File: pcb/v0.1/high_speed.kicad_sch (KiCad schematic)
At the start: 14 parts, among them J1 USB_C_Receptacle_fw, J2 USB_C_Receptacle_fw, J3 690-019-298-412, J4 Conn_01x22_Female, U1 AP22653W6, U2 RT9742SNGV

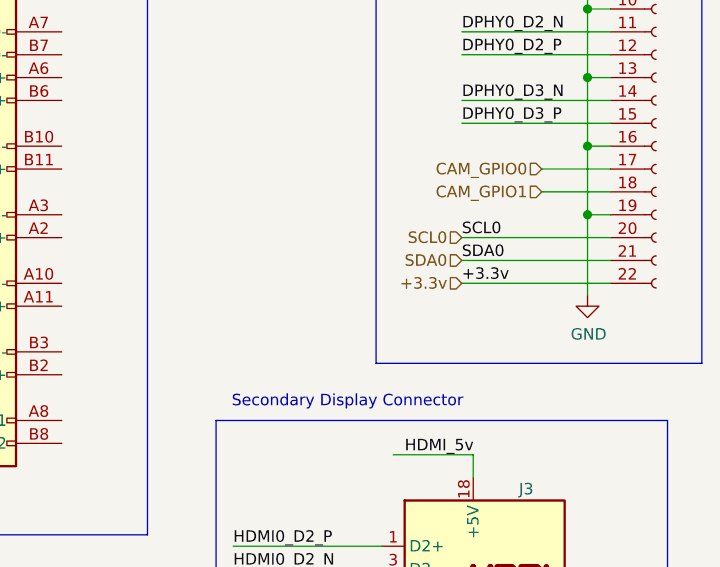
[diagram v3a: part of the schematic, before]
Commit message: Clean up main page and power rails
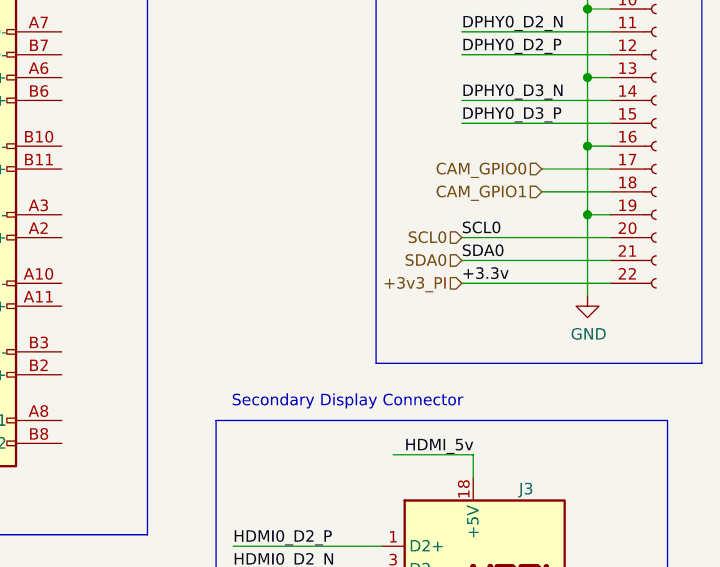
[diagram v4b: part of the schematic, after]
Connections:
- net +3.3v renamed +3v3_PI
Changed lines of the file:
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@@
 		)
 	)
-	(hierarchical_label "+3.3v"
+	(hierarchical_label "+3v3_PI"
 		(shape input)
 		(at 254 76.2 180)

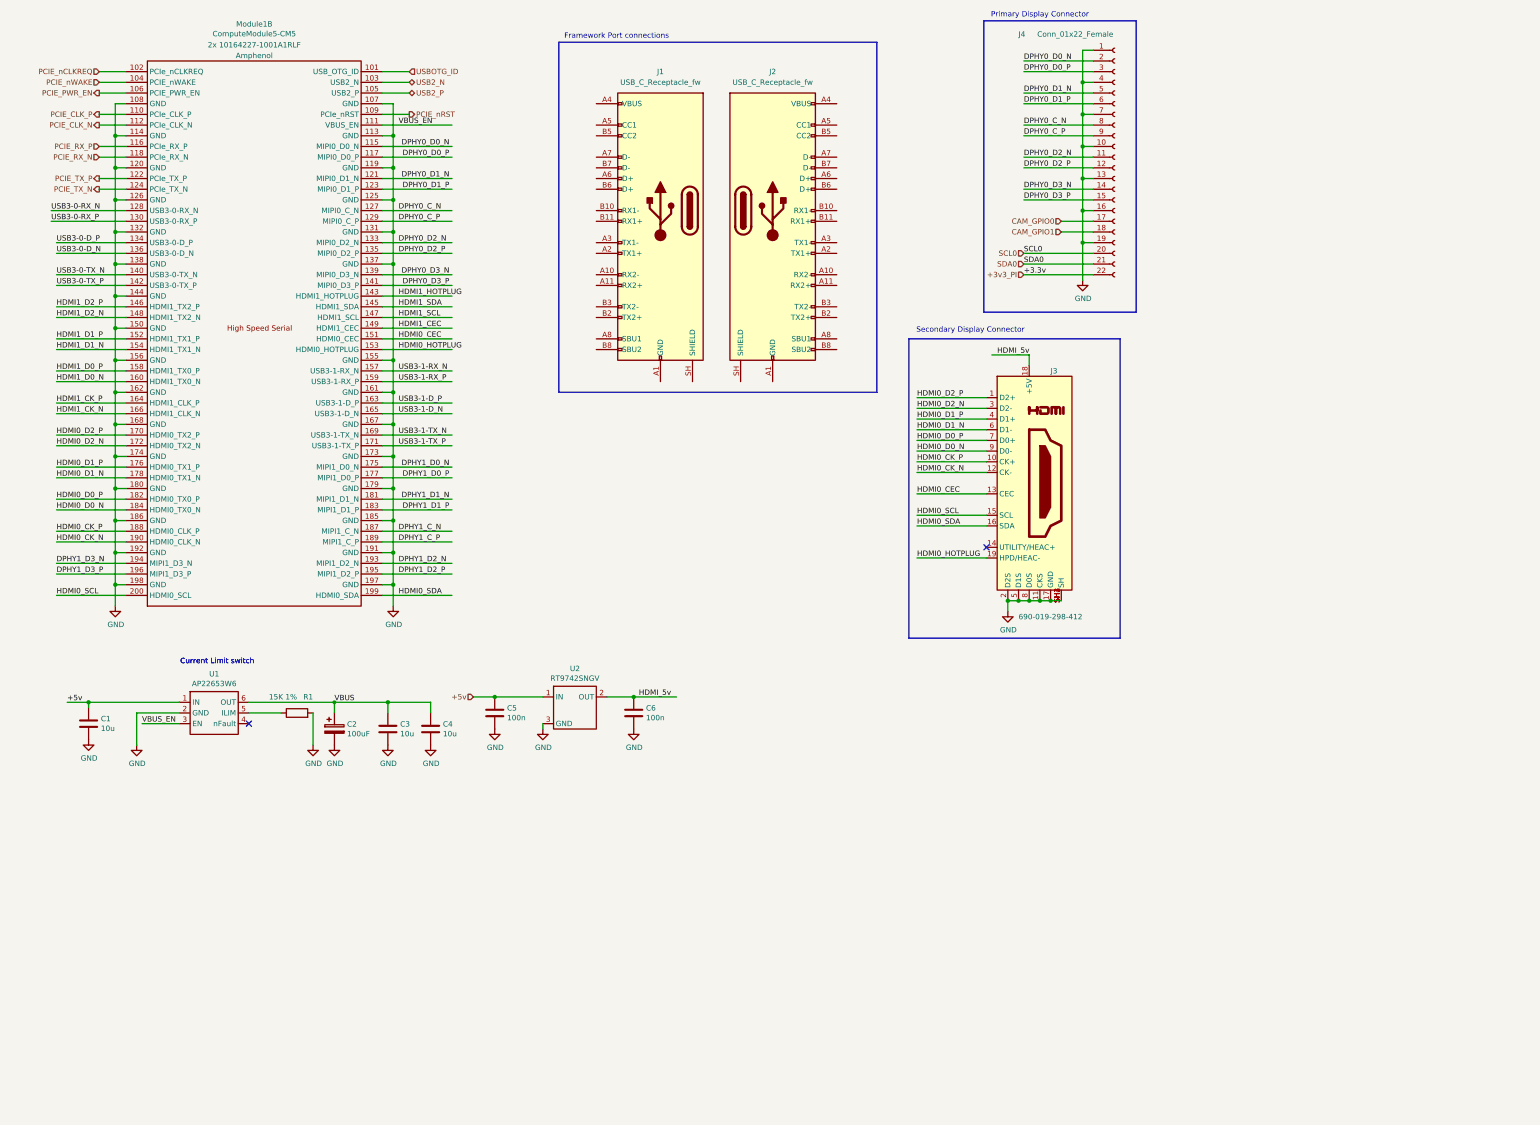
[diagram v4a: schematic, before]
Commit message: Add pullup for nRESET of the nRF.
Also re-annotated all of the symbol numbers as they were starting to get
out of hand.
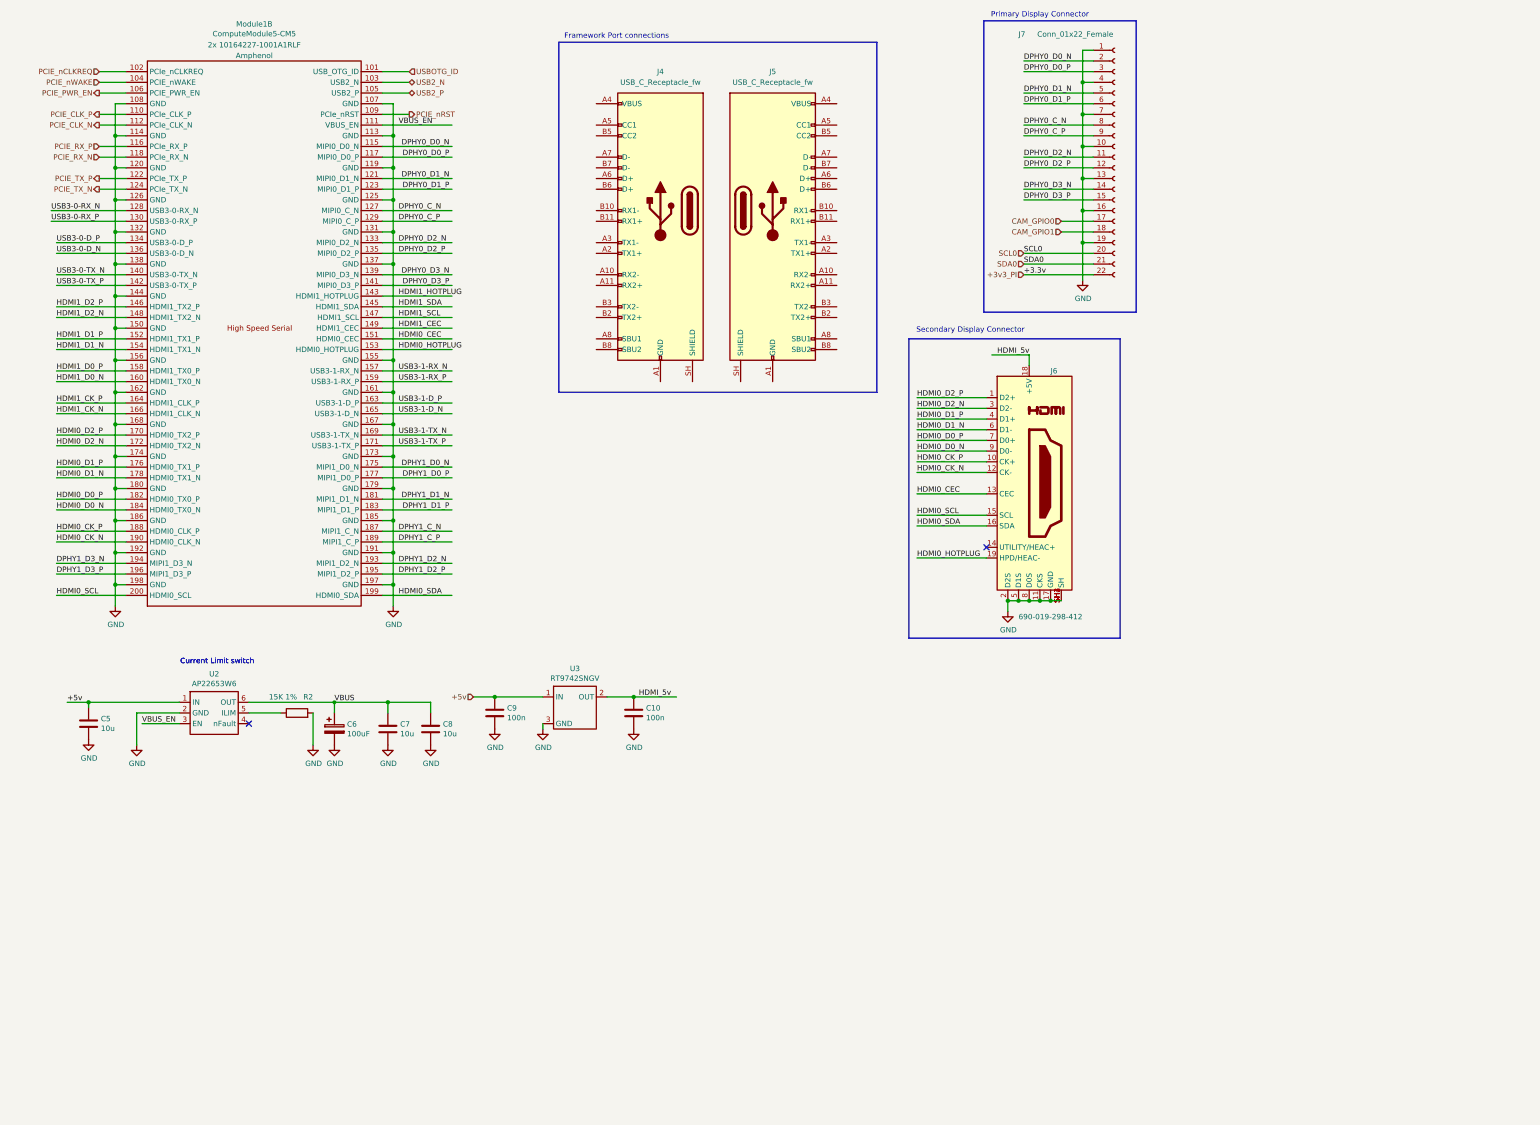
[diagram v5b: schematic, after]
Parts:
- renumbered C6 to C10, C1 to C5, C2 to C6, C3 to C7, C4 to C8, C5 to C9, J1 to J4, J2 to J5, J3 to J6, J4 to J7, R1 to R2, U1 to U2, U2 to U3
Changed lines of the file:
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@@
 		(in_pos_files yes)
 		(dnp no)
-		(property "Reference" "#PWR05"
+		(property "Reference" "#PWR010"
 			(at 90.17 194.31 0)
 			(hide yes)
@@
 			(project "mainboard"
 				(path "/5b8aa782-5c3d-43e7-a869-3bd000015f52/8e613e76-cfa9-4d70-9fba-6dbea9bbdbc9"
-					(reference "#PWR05")
+					(reference "#PWR010")
 					(unit 1)
 				)
@@
 		(in_pos_files yes)
 		(dnp no)
-		(property "Reference" "#PWR01"
+		(property "Reference" "#PWR06"
 			(at 31.75 193.04 0)
 			(hide yes)
@@
 			(project "mainboard"
 				(path "/5b8aa782-5c3d-43e7-a869-3bd000015f52/8e613e76-cfa9-4d70-9fba-6dbea9bbdbc9"
-					(reference "#PWR01")
+					(reference "#PWR06")
 					(unit 1)
 				)
@@
 		(in_pos_files yes)
 		(dnp no)
-		(property "Reference" "#PWR010"
+		(property "Reference" "#PWR015"
 			(at 139.7 190.5 0)
 			(hide yes)
@@
 			(project "mainboard"
 				(path "/5b8aa782-5c3d-43e7-a869-3bd000015f52/8e613e76-cfa9-4d70-9fba-6dbea9bbdbc9"
-					(reference "#PWR010")
+					(reference "#PWR015")
 					(unit 1)
 				)
@@
 		(in_pos_files yes)
 		(dnp no)
-		(property "Reference" "J4"
+		(property "Reference" "J7"
 			(at 252.73 19.05 0)
 			(show_name no)
@@
 			(project "mainboard"
 				(path "/5b8aa782-5c3d-43e7-a869-3bd000015f52/8e613e76-cfa9-4d70-9fba-6dbea9bbdbc9"
-					(reference "J4")
+					(reference "J7")
 					(unit 1)
 				)
@@
 		(in_pos_files yes)
 		(dnp no)
-		(property "Reference" "J1"
+		(property "Reference" "J4"
 			(at 167.64 27.94 0)
 			(show_name no)
@@
 			(project "mainboard"
 				(path "/5b8aa782-5c3d-43e7-a869-3bd000015f52/8e613e76-cfa9-4d70-9fba-6dbea9bbdbc9"
-					(reference "J1")
+					(reference "J4")
 					(unit 1)
 				)
@@
 		(in_pos_files yes)
 		(dnp no)
-		(property "Reference" "#PWR03"
+		(property "Reference" "#PWR08"
 			(at 43.18 194.31 0)
 			(hide yes)
@@
 			(project "mainboard"
 				(path "/5b8aa782-5c3d-43e7-a869-3bd000015f52/8e613e76-cfa9-4d70-9fba-6dbea9bbdbc9"
-					(reference "#PWR03")
+					(reference "#PWR08")
 					(unit 1)
 				)
@@
 		(in_pos_files yes)
 		(dnp no)
-		(property "Reference" "C4"
+		(property "Reference" "C8"
 			(at 115.951 182.9816 0)
 			(show_name no)
@@
 			(project "mainboard"
 				(path "/5b8aa782-5c3d-43e7-a869-3bd000015f52/8e613e76-cfa9-4d70-9fba-6dbea9bbdbc9"
-					(reference "C4")
+					(reference "C8")
 					(unit 1)
 				)
@@
 		(in_pos_files yes)
 		(dnp no)
-		(property "Reference" "#PWR08"
+		(property "Reference" "#PWR013"
 			(at 113.03 194.31 0)
 			(hide yes)
@@
 			(project "mainboard"
 				(path "/5b8aa782-5c3d-43e7-a869-3bd000015f52/8e613e76-cfa9-4d70-9fba-6dbea9bbdbc9"
-					(reference "#PWR08")
+					(reference "#PWR013")
 					(unit 1)
 				)
@@
 		(in_pos_files yes)
 		(dnp no)
-		(property "Reference" "#PWR013"
+		(property "Reference" "#PWR018"
 			(at 267.97 83.82 0)
 			(hide yes)
@@
 			(project "mainboard"
 				(path "/5b8aa782-5c3d-43e7-a869-3bd000015f52/8e613e76-cfa9-4d70-9fba-6dbea9bbdbc9"
-					(reference "#PWR013")
+					(reference "#PWR018")
 					(unit 1)
 				)
@@
 		(in_pos_files yes)
 		(dnp no)
-		(property "Reference" "U1"
+		(property "Reference" "U2"
 			(at 61.595 171.069 0)
 			(show_name no)
@@
 			(project "mainboard"
 				(path "/5b8aa782-5c3d-43e7-a869-3bd000015f52/8e613e76-cfa9-4d70-9fba-6dbea9bbdbc9"
-					(reference "U1")
+					(reference "U2")
 					(unit 1)
 				)
@@
 		(in_pos_files yes)
 		(dnp no)
-		(property "Reference" "R1"
+		(property "Reference" "R2"
 			(at 85.09 176.53 90)
 			(show_name no)
@@
 			(project "mainboard"
 				(path "/5b8aa782-5c3d-43e7-a869-3bd000015f52/8e613e76-cfa9-4d70-9fba-6dbea9bbdbc9"
-					(reference "R1")
+					(reference "R2")
 					(unit 1)
 				)
@@
 		(in_pos_files yes)
 		(dnp no)
-		(property "Reference" "J3"
+		(property "Reference" "J6"
 			(at 260.35 99.06 0)
 			(show_name no)
@@
 			(project "mainboard"
 				(path "/5b8aa782-5c3d-43e7-a869-3bd000015f52/8e613e76-cfa9-4d70-9fba-6dbea9bbdbc9"
-					(reference "J3")
+					(reference "J6")
 					(unit 1)
 				)
@@
 		(in_pos_files yes)
 		(dnp no)
-		(property "Reference" "C6"
+		(property "Reference" "C10"
 			(at 164.211 179.1716 0)
 			(show_name no)
@@
 			(project "mainboard"
 				(path "/5b8aa782-5c3d-43e7-a869-3bd000015f52/8e613e76-cfa9-4d70-9fba-6dbea9bbdbc9"
-					(reference "C6")
+					(reference "C10")
 					(unit 1)
 				)
@@
 		(in_pos_files yes)
 		(dnp no)
-		(property "Reference" "#PWR07"
+		(property "Reference" "#PWR012"
 			(at 104.14 161.29 0)
 			(hide yes)
@@
 			(project "mainboard"
 				(path "/5b8aa782-5c3d-43e7-a869-3bd000015f52/8e613e76-cfa9-4d70-9fba-6dbea9bbdbc9"
-					(reference "#PWR07")
+					(reference "#PWR012")
 					(unit 1)
 				)
@@
 		(in_pos_files yes)
 		(dnp no)
-		(property "Reference" "C1"
+		(property "Reference" "C5"
 			(at 34.671 181.7116 0)
 			(show_name no)
@@
 			(project "mainboard"
 				(path "/5b8aa782-5c3d-43e7-a869-3bd000015f52/8e613e76-cfa9-4d70-9fba-6dbea9bbdbc9"
-					(reference "C1")
+					(reference "C5")
 					(unit 1)
 				)
@@
 		(dnp no)
 		(fields_autoplaced yes)
-		(property "Reference" "J2"
+		(property "Reference" "J5"
 			(at 194.31 27.94 0)
 			(show_name no)
@@
 			(project "mainboard"
 				(path "/5b8aa782-5c3d-43e7-a869-3bd000015f52/8e613e76-cfa9-4d70-9fba-6dbea9bbdbc9"
-					(reference "J2")
+					(reference "J5")
 					(unit 1)
 				)
@@
 		(in_pos_files yes)
 		(dnp no)
-		(property "Reference" "#PWR06"
+		(property "Reference" "#PWR011"
 			(at 102.87 194.31 0)
 			(hide yes)
@@
 			(project "mainboard"
 				(path "/5b8aa782-5c3d-43e7-a869-3bd000015f52/8e613e76-cfa9-4d70-9fba-6dbea9bbdbc9"
-					(reference "#PWR06")
+					(reference "#PWR011")
 					(unit 1)
 				)
@@
 		(in_pos_files yes)
 		(dnp no)
-		(property "Reference" "C5"
+		(property "Reference" "C9"
 			(at 131.191 179.1716 0)
 			(show_name no)
@@
 			(project "mainboard"
 				(path "/5b8aa782-5c3d-43e7-a869-3bd000015f52/8e613e76-cfa9-4d70-9fba-6dbea9bbdbc9"
-					(reference "C5")
+					(reference "C9")
 					(unit 1)
 				)
@@
 		(in_pos_files yes)
 		(dnp no)
-		(property "Reference" "U2"
+		(property "Reference" "U3"
 			(at 147.32 169.799 0)
 			(show_name no)
@@
 			(project "mainboard"
 				(path "/5b8aa782-5c3d-43e7-a869-3bd000015f52/8e613e76-cfa9-4d70-9fba-6dbea9bbdbc9"
-					(reference "U2")
+					(reference "U3")
 					(unit 1)
 				)
@@
 		(in_pos_files yes)
 		(dnp no)
-		(property "Reference" "#PWR04"
+		(property "Reference" "#PWR09"
 			(at 85.09 194.31 0)
 			(hide yes)
@@
 			(project "mainboard"
 				(path "/5b8aa782-5c3d-43e7-a869-3bd000015f52/8e613e76-cfa9-4d70-9fba-6dbea9bbdbc9"
-					(reference "#PWR04")
+					(reference "#PWR09")
 					(unit 1)
 				)
@@
 		(in_pos_files yes)
 		(dnp no)
-		(property "Reference" "#PWR012"
+		(property "Reference" "#PWR017"
 			(at 250.19 162.56 0)
 			(hide yes)
@@
 			(project "mainboard"
 				(path "/5b8aa782-5c3d-43e7-a869-3bd000015f52/8e613e76-cfa9-4d70-9fba-6dbea9bbdbc9"
-					(reference "#PWR012")
+					(reference "#PWR017")
 					(unit 1)
 				)
@@
 		(in_pos_files yes)
 		(dnp no)
-		(property "Reference" "C2"
+		(property "Reference" "C6"
 			(at 93.1672 183.007 0)
 			(show_name no)
@@
 			(project "mainboard"
 				(path "/5b8aa782-5c3d-43e7-a869-3bd000015f52/8e613e76-cfa9-4d70-9fba-6dbea9bbdbc9"
-					(reference "C2")
+					(reference "C6")
 					(unit 1)
 				)
@@
 		(in_pos_files yes)
 		(dnp no)
-		(property "Reference" "#PWR09"
+		(property "Reference" "#PWR014"
 			(at 128.27 190.5 0)
 			(hide yes)
@@
 			(project "mainboard"
 				(path "/5b8aa782-5c3d-43e7-a869-3bd000015f52/8e613e76-cfa9-4d70-9fba-6dbea9bbdbc9"
-					(reference "#PWR09")
+					(reference "#PWR014")
 					(unit 1)
 				)
@@
 		(in_pos_files yes)
 		(dnp no)
-		(property "Reference" "#PWR011"
+		(property "Reference" "#PWR016"
 			(at 161.29 190.5 0)
 			(hide yes)
@@
 			(project "mainboard"
 				(path "/5b8aa782-5c3d-43e7-a869-3bd000015f52/8e613e76-cfa9-4d70-9fba-6dbea9bbdbc9"
-					(reference "#PWR011")
+					(reference "#PWR016")
 					(unit 1)
 				)
@@
 		(in_pos_files yes)
 		(dnp no)
-		(property "Reference" "C3"
+		(property "Reference" "C7"
 			(at 105.791 182.9816 0)
 			(show_name no)
@@
 			(project "mainboard"
 				(path "/5b8aa782-5c3d-43e7-a869-3bd000015f52/8e613e76-cfa9-4d70-9fba-6dbea9bbdbc9"
-					(reference "C3")
+					(reference "C7")
 					(unit 1)
 				)
@@
 		(in_pos_files yes)
 		(dnp no)
-		(property "Reference" "#PWR02"
+		(property "Reference" "#PWR07"
 			(at 38.1 161.29 0)
 			(hide yes)
@@
 			(project "mainboard"
 				(path "/5b8aa782-5c3d-43e7-a869-3bd000015f52/8e613e76-cfa9-4d70-9fba-6dbea9bbdbc9"
-					(reference "#PWR02")
+					(reference "#PWR07")
 					(unit 1)
 				)
